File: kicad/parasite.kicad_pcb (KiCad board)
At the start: 2 copper layers, 22 x 126.4 mm, 33 parts, among them Q1 MMBT3904, Q2 MMBT3904, Q3 AO3407, Q4 Q_Photo_NPN, U1 E73-2G4M08S1C-52840, U2 SHTC3, Y1 32.768kHz

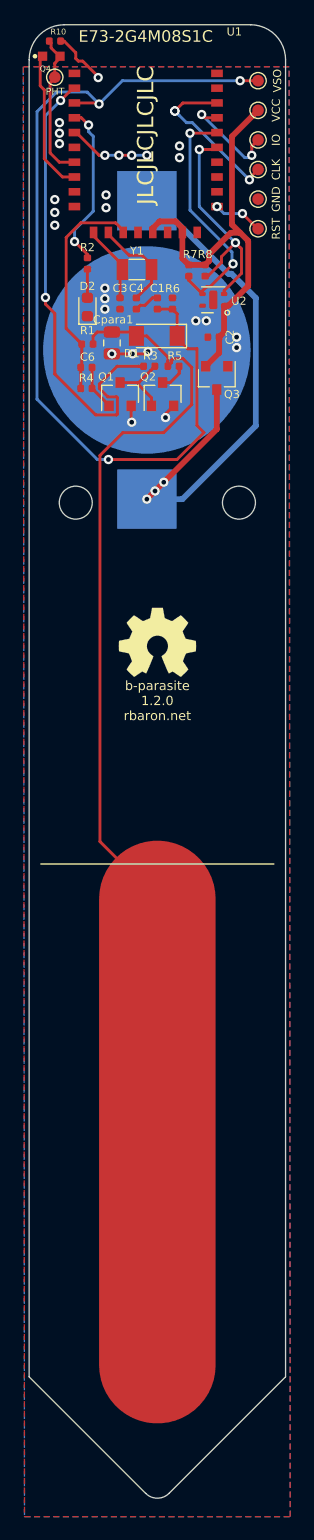
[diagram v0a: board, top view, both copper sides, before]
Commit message: added picoblade connector
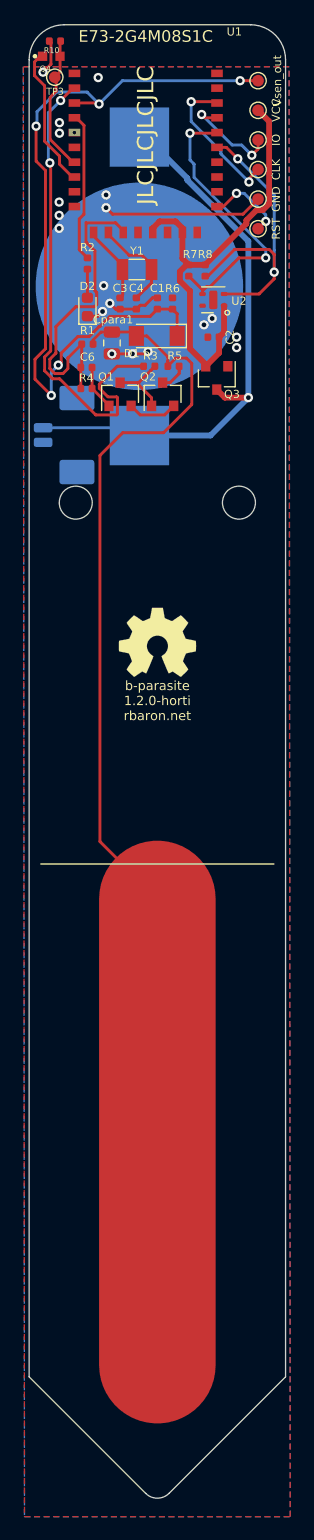
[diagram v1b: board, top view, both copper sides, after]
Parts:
- added J1: Conn_01x02_Male, Connector_Molex:Molex_PicoBlade_53261-0271_1x02-1MP_P1.25mm_Horizontal, B.Cu at (60.6, 62.2)
- TP4: value VSO -> Vsen_out
- moved BT1 5.50 mm to (66.5, 49.4)
- turned R10 to 0 degrees
- renumbered PHT to TP3
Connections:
- U1 pad 1: Net-(U1-Pad1) -> unconnected-(U1-Pad1)
- U1 pad 10: Net-(U1-Pad10) -> unconnected-(U1-Pad10)
- U1 pad 17: Net-(U1-Pad17) -> unconnected-(U1-Pad17)
- U1 pad 25: Net-(U1-Pad25) -> unconnected-(U1-Pad25)
- U1 pad 27: Net-(U1-Pad27) -> unconnected-(U1-Pad27)
- U1 pad 29: Net-(U1-Pad29) -> unconnected-(U1-Pad29)
- U1 pad 31: Net-(U1-Pad31) -> unconnected-(U1-Pad31)
- U1 pad 41: Net-(U1-Pad41) -> unconnected-(U1-Pad41)
- U1 pad 43: Net-(U1-Pad43) -> unconnected-(U1-Pad43)
- U1 pad 6: Net-(U1-Pad6) -> unconnected-(U1-Pad6)
- U1 pad 9: Net-(U1-Pad9) -> unconnected-(U1-Pad9)
- U2 pad 5: Net-(U2-Pad5) -> unconnected-(U2-Pad5)
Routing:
- net /SENS_OUT: track 78.6 -> 66.3 mm, vias 3 -> 5
- net GND: track 20.4 -> 30.5 mm, vias 27 -> 19
- net /PWM: track 19.4 -> 27.2 mm
- net /SCL: track 20.2 -> 27.2 mm
- net /SDA: track 20.9 -> 24.5 mm
- net Net-(BT1-Pad1): track 47.6 -> 50.8 mm, vias 3 -> 1
- net Net-(TP5-Pad1): track 4.31 -> 6.90 mm
- net +3V0: track 37.8 -> 40.2 mm
- net Net-(TP2-Pad1): track 14.5 -> 12.4 mm, vias 3 -> 2
- net /LED: track 14.2 -> 12.7 mm, vias 2 -> 0
- net /PHOTO_OUT: track 12.6 -> 11.4 mm
- net Net-(C3-Pad1): track 6.72 -> 5.99 mm
- net Net-(C4-Pad2): track 8.33 -> 7.76 mm
- net /Csen+: track 104.6 -> 104.1 mm
- net /PHOTO_V: track 12.4 -> 11.9 mm
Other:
- board text added: "b-parasite 1.2.0-horti rbaron.net"
- board text removed: "b-parasite 1.2.0 rbaron.net"
